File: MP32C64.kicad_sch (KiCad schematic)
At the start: 19 parts, among them CN1 AUDIO_IN, CN2 C64_CASS_PORT, SW1 SW_INVERT, U1 CD4069

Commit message: Tidy up
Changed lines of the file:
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@@
 		(fields_autoplaced yes)
 		(property "Reference" "C3"
-			(at 30.48 167.6399 0)
+			(at 22.86 167.6399 0)
 			(effects
 				(font
 					(size 1.27 1.27)
 				)
-				(justify right)
+				(justify left)
 			)
 		)
 		(property "Value" "100n"
-			(at 30.48 170.1799 0)
+			(at 22.86 170.1799 0)
 			(effects
 				(font
 					(size 1.27 1.27)
 				)
-				(justify right)
+				(justify left)
 			)
 		)

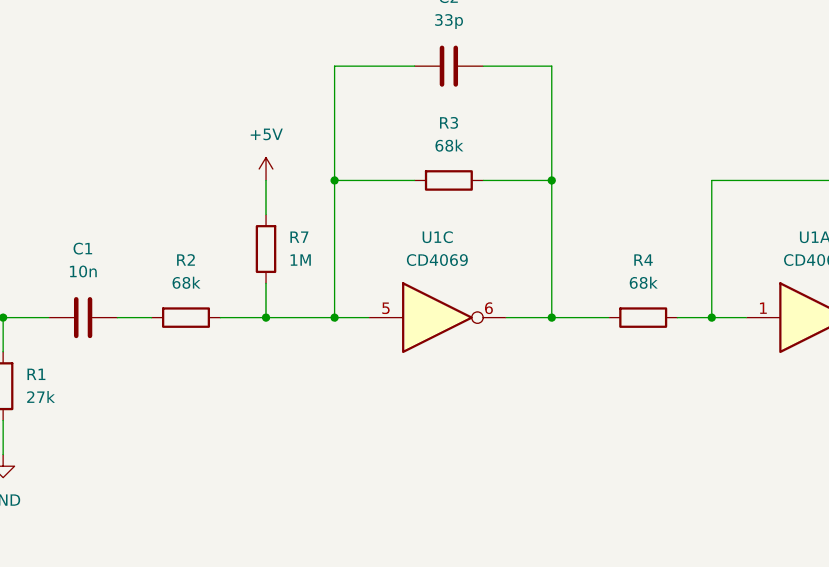
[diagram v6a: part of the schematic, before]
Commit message: Fix resistor values & add renders
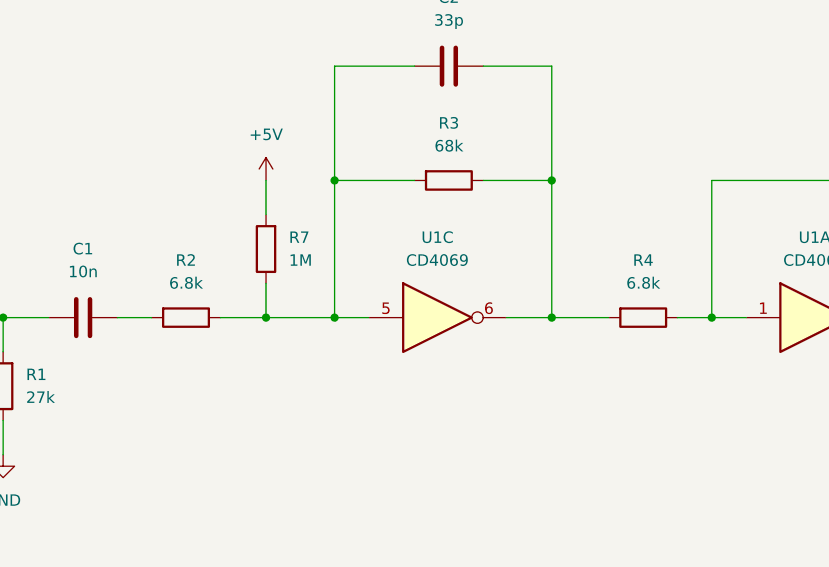
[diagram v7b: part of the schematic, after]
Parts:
- R2, R4: value 68k -> 6.8k
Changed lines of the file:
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@@
 	(title_block
 		(title "MP32C64")
-		(date "2025-03-25")
+		(date "2025-06-30")
 		(rev "1git")
 		(company "SukkoPera")
@@
 			)
 		)
-		(property "Value" "68k"
+		(property "Value" "6.8k"
 			(at 58.42 52.07 90)
 			(effects
@@
 			)
 		)
-		(property "Value" "68k"
+		(property "Value" "6.8k"
 			(at 109.22 52.07 90)
 			(effects
